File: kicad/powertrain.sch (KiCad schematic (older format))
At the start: 72 parts, among them P6 WR-TBL_691313710002, P7 CONN_01X02, P8 WR-TBL_691313710002, Q1 2N7002, U10 IFX007T, U11 74xx08, U5 LM358, U6 IFX007T, U7 IFX007T, U8 LM358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

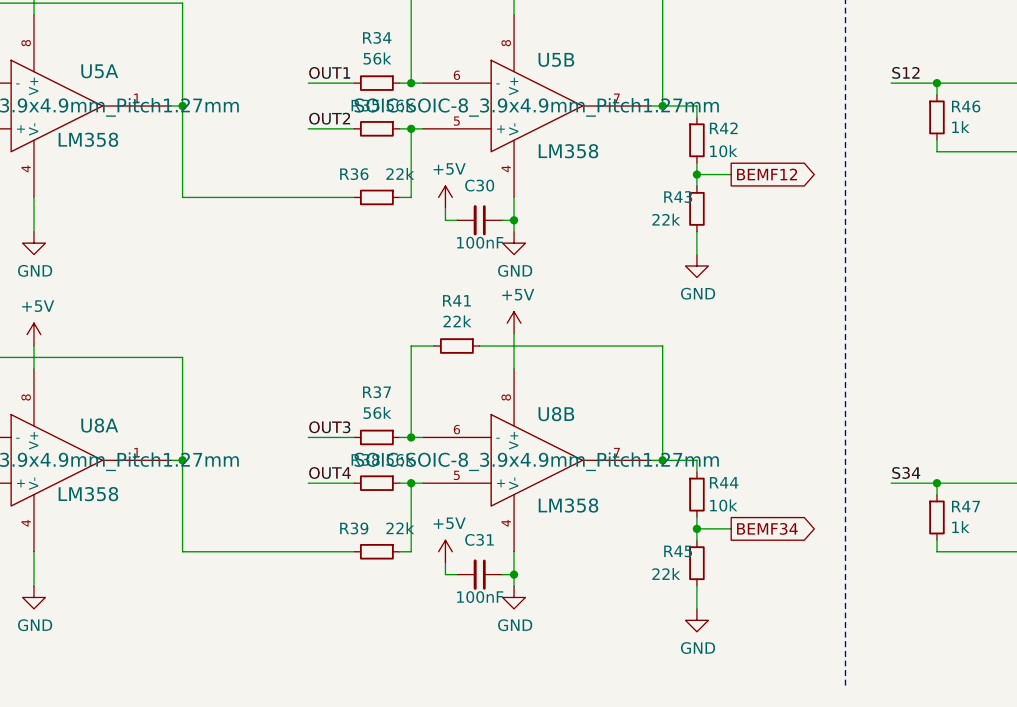
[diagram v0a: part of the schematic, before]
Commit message: added capacitors
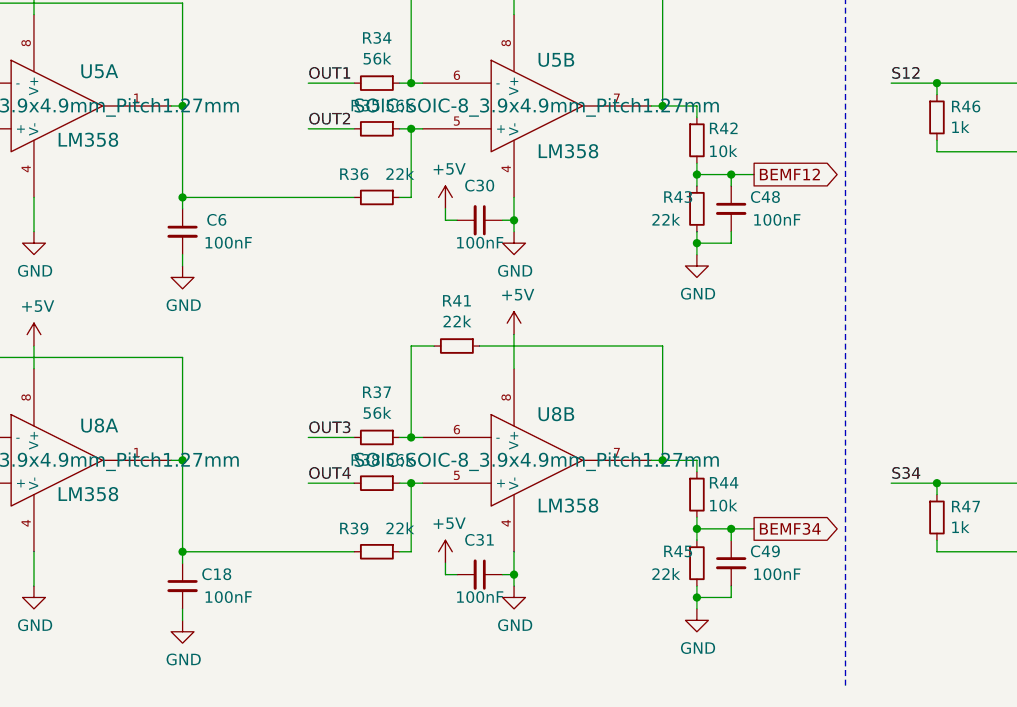
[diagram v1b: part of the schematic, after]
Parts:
- added C18, C48, C49, C6: 100nF, capacitors:C_0603, symbol devices:C_0603
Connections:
- net BEMF12: now also C48.1
- net BEMF34: now also C49.1
- net GND: now also C18.2, C48.2, C49.2, C6.2
- net at R36.2, U5.1, U5.2 (-): now also C6.1
- net at R39.2, U8.1, U8.2 (-): now also C18.1
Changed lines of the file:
@@
 	1    0    0    -1
 $EndComp
-Text GLabel 4950 7050 2    50   Output ~ 0
+Text GLabel 5050 7050 2    50   Output ~ 0
 BEMF34
 Connection ~ 4650 6750
@@
 	4800 6800 4800 6750
 Wire Wire Line
-	4800 7400 4800 7300
+	4800 7400 4800 7350
 Connection ~ 4000 7250
 Wire Wire Line
@@
 	1    0    0    -1
 $EndComp
-Wire Wire Line
-	4800 7050 4950 7050
 Wire Wire Line
 	4650 6250 3850 6250
@@
 	1    0    0    -1
 $EndComp
-Text GLabel 4950 5500 2    50   Output ~ 0
+Text GLabel 5050 5500 2    50   Output ~ 0
 BEMF12
 Connection ~ 4650 5200
@@
 	4800 5250 4800 5200
 Wire Wire Line
-	4800 5850 4800 5750
+	4800 5850 4800 5800
 Connection ~ 4000 5700
 Wire Wire Line
@@
 	1    0    0    -1
 $EndComp
+$Comp
+L devices:C_0603 C49
+U 1 1 5F6F6DBC
+P 4950 7200
+F 0 "C49" H 5100 7250 50  0000 C CNN
+F 1 "100nF" H 5150 7150 50  0000 C CNN
+F 2 "capacitors:C_0603" H 4950 7050 50  0001 C CNN
+F 3 "" H 4950 7200 50  0000 C CNN
+	1    4950 7200
+	1    0    0    -1
+$EndComp
+$Comp
+L devices:C_0603 C48
+U 1 1 5F7130B1
+P 4950 5650
+F 0 "C48" H 5100 5700 50  0000 C CNN
+F 1 "100nF" H 5150 5600 50  0000 C CNN
+F 2 "capacitors:C_0603" H 4950 5500 50  0001 C CNN
+F 3 "" H 4950 5650 50  0000 C CNN
+	1    4950 5650
+	1    0    0    -1
+$EndComp
+$Comp
+L devices:C_0603 C6
+U 1 1 5F72E83B
+P 2550 5750
+F 0 "C6" H 2700 5800 50  0000 C CNN
+F 1 "100nF" H 2750 5700 50  0000 C CNN
+F 2 "capacitors:C_0603" H 2550 5600 50  0001 C CNN
+F 3 "" H 2550 5750 50  0000 C CNN
+	1    2550 5750
+	1    0    0    -1
+$EndComp
+$Comp
+L devices:C_0603 C18
+U 1 1 5F749F41
+P 2550 7300
+F 0 "C18" H 2700 7350 50  0000 C CNN
+F 1 "100nF" H 2750 7250 50  0000 C CNN
+F 2 "capacitors:C_0603" H 2550 7150 50  0001 C CNN
+F 3 "" H 2550 7300 50  0000 C CNN
+	1    2550 7300
+	1    0    0    -1
+$EndComp
+Wire Wire Line
+	2550 7200 2550 7150
+Connection ~ 2550 7150
+Wire Wire Line
+	2550 5650 2550 5600
+Connection ~ 2550 5600
+Wire Wire Line
+	4950 5550 4950 5500
+Connection ~ 4950 5500
+Wire Wire Line
+	4950 5500 5050 5500
+Wire Wire Line
+	4800 5800 4950 5800
+Wire Wire Line
+	4950 5800 4950 5750
+Connection ~ 4800 5800
+Wire Wire Line
+	4800 5800 4800 5750
+Wire Wire Line
+	4800 7050 4950 7050
+Wire Wire Line
+	4950 7100 4950 7050
+Connection ~ 4950 7050
+Wire Wire Line
+	4950 7050 5050 7050
+Wire Wire Line
+	4950 7300 4950 7350
+Wire Wire Line
+	4950 7350 4800 7350
+Connection ~ 4800 7350
+Wire Wire Line
+	4800 7350 4800 7300
+$Comp
+L power-supply:GND #PWR0142
+U 1 1 5F82F73A
+P 2550 7450
+F 0 "#PWR0142" H 2550 7200 50  0001 C CNN
+F 1 "GND" H 2555 7277 50  0000 C CNN
+F 2 "" H 2550 7450 50  0000 C CNN
+F 3 "" H 2550 7450 50  0000 C CNN
+	1    2550 7450
+	1    0    0    -1
+$EndComp
+$Comp
+L power-supply:GND #PWR0147
+U 1 1 5F84D103
+P 2550 5900
+F 0 "#PWR0147" H 2550 5650 50  0001 C CNN
+F 1 "GND" H 2555 5727 50  0000 C CNN
+F 2 "" H 2550 5900 50  0000 C CNN
+F 3 "" H 2550 5900 50  0000 C CNN
+	1    2550 5900
+	1    0    0    -1
+$EndComp
+Wire Wire Line
+	2550 5900 2550 5850
+Wire Wire Line
+	2550 7450 2550 7400
 $EndSCHEMATC

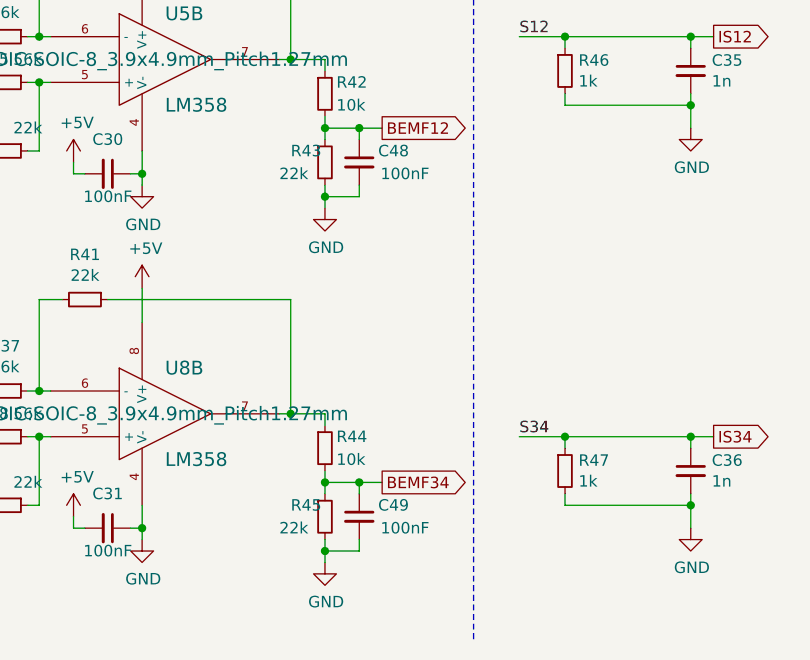
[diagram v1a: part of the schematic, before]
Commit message: added leds, updated capacitor values and changed silkscreen
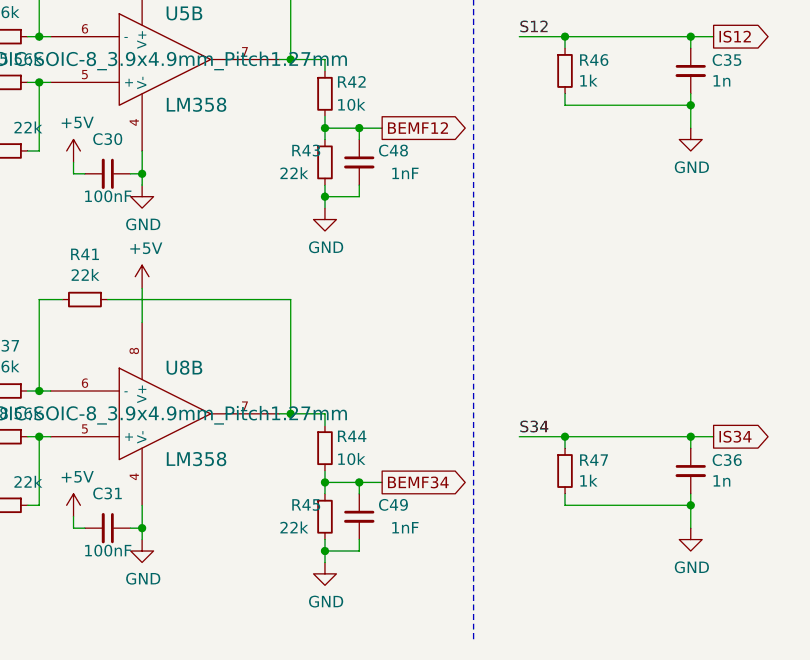
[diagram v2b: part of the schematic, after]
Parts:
- C48, C49: value 100nF -> 1nF
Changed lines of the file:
@@
 P 4950 7200
 F 0 "C49" H 5100 7250 50  0000 C CNN
-F 1 "100nF" H 5150 7150 50  0000 C CNN
+F 1 "1nF" H 5150 7150 50  0000 C CNN
 F 2 "capacitors:C_0603" H 4950 7050 50  0001 C CNN
 F 3 "" H 4950 7200 50  0000 C CNN
@@
 P 4950 5650
 F 0 "C48" H 5100 5700 50  0000 C CNN
-F 1 "100nF" H 5150 5600 50  0000 C CNN
+F 1 "1nF" H 5150 5600 50  0000 C CNN
 F 2 "capacitors:C_0603" H 4950 5500 50  0001 C CNN
 F 3 "" H 4950 5650 50  0000 C CNN

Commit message: bom update
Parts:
- C35, C36: value 1n -> 1nF
- C5: value 100 nF -> 100nF
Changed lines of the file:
@@
 P 6400 5250
 F 0 "C35" H 6492 5296 50  0000 L CNN
-F 1 "1n" H 6492 5205 50  0000 L CNN
+F 1 "1nF" H 6492 5205 50  0000 L CNN
 F 2 "capacitors:C_0603" H 6400 5100 50  0001 C CNN
 F 3 "" H 6400 5250 50  0000 C CNN
@@
 P 6400 7000
 F 0 "C36" H 6492 7046 50  0000 L CNN
-F 1 "1n" H 6492 6955 50  0000 L CNN
+F 1 "1nF" H 6492 6955 50  0000 L CNN
 F 2 "capacitors:C_0603" H 6400 6850 50  0001 C CNN
 F 3 "" H 6400 7000 50  0000 C CNN
@@
 P 8650 4900
 F 0 "C5" H 8742 4946 50  0000 L CNN
-F 1 "100 nF" H 8742 4855 50  0000 L CNN
+F 1 "100nF" H 8742 4855 50  0000 L CNN
 F 2 "capacitors:C_0603" H 8650 4750 50  0001 C CNN
 F 3 "" H 8650 4900 50  0000 C CNN

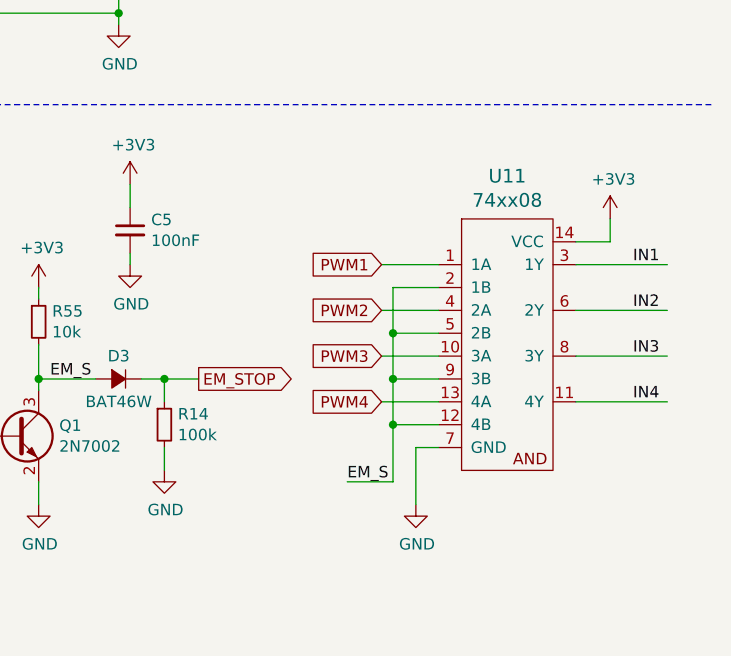
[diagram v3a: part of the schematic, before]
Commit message: improved emergency stop for breaking
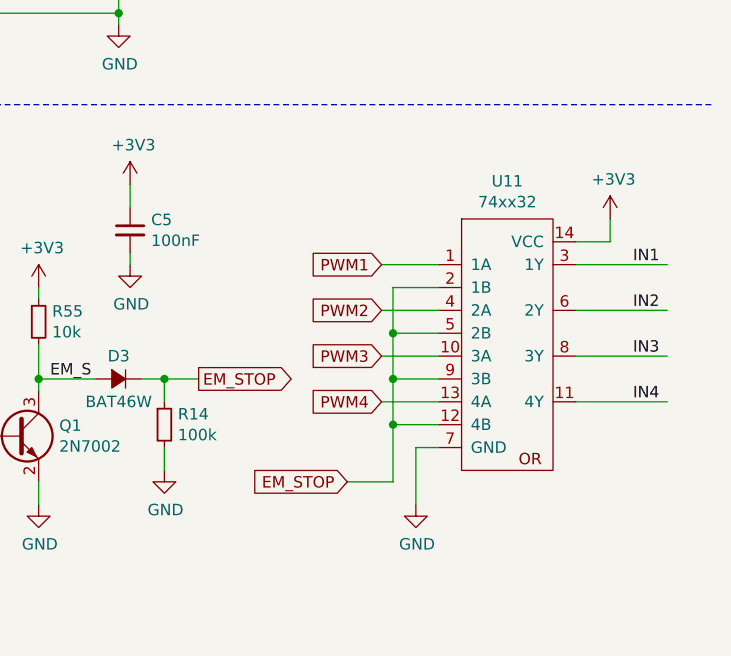
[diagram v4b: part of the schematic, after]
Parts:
- removed U11: 74xx08, SOIC:SOIC-14_3.9x8.7mm_Pitch1.27mm, symbol IC_logic:74xx08
- added U11: 74xx32, SOIC:SOIC-14_3.9x8.7mm_Pitch1.27mm, symbol IC_logic:74xx32
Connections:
- net +3V3: now also U11.14 (VCC)
- net EM_STOP: now also U11.12 (4B), U11.2 (1B), U11.5 (2B), U11.9 (3B)
- net GND: now also U11.7 (GND)
- net IN1: now also U11.3 (1Y)
- net IN2: now also U11.6 (2Y)
- net IN3: now also U11.8 (3Y)
- net IN4: now also U11.11 (4Y)
- net PWM1: now also U11.1 (1A)
- net PWM2: now also U11.4 (2A)
- net PWM3: now also U11.10 (3A)
- net PWM4: now also U11.13 (4A)
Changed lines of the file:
@@
 Text Label 6350 3100 0    50   ~ 0
 IN4
-$Comp
-L IC_logic:74xx08 U11
-U 1 1 5EF16DC4
-P 10100 5350
-F 0 "U11" H 10300 6037 60  0000 C CNN
-F 1 "74xx08" H 10300 5931 60  0000 C CNN
-F 2 "SOIC:SOIC-14_3.9x8.7mm_Pitch1.27mm" H 10400 5200 60  0001 C CNN
-F 3 "" H 10100 5350 60  0000 C CNN
-	1    10100 5350
-	1    0    0    -1
-$EndComp
 Text GLabel 9750 5050 0    50   Input ~ 0
 PWM1
@@
 Wire Wire Line
 	9600 6000 9800 6000
-Text Label 9600 6000 0    50   ~ 0
-EM_S
 $Comp
 L devices:R_0603 R14
@@
 Wire Wire Line
 	2550 7450 2550 7400
+Text GLabel 9600 6000 0    50   Input ~ 0
+EM_STOP
+$Comp
+L IC_logic:74xx32 U11
+U 1 1 5F7E0FEC
+P 10250 5950
+F 0 "U11" H 10300 7215 50  0000 C CNN
+F 1 "74xx32" H 10300 7124 50  0000 C CNN
+F 2 "SOIC:SOIC-14_3.9x8.7mm_Pitch1.27mm" H 10250 5950 50  0001 C CNN
+F 3 "" H 10250 5950 50  0001 C CNN
+	1    10250 5950
+	1    0    0    -1
+$EndComp
 $EndSCHEMATC

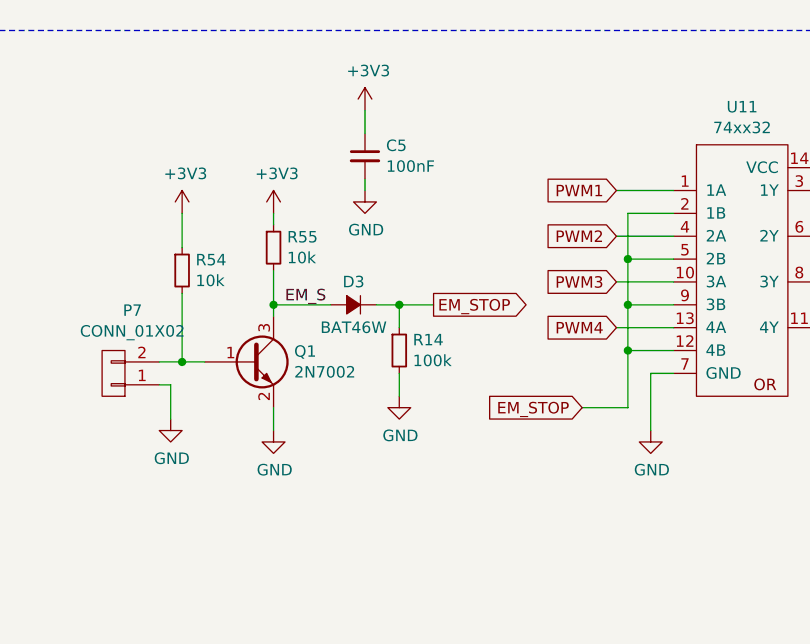
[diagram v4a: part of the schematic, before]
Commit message: improved emergency stop circuit for breaking
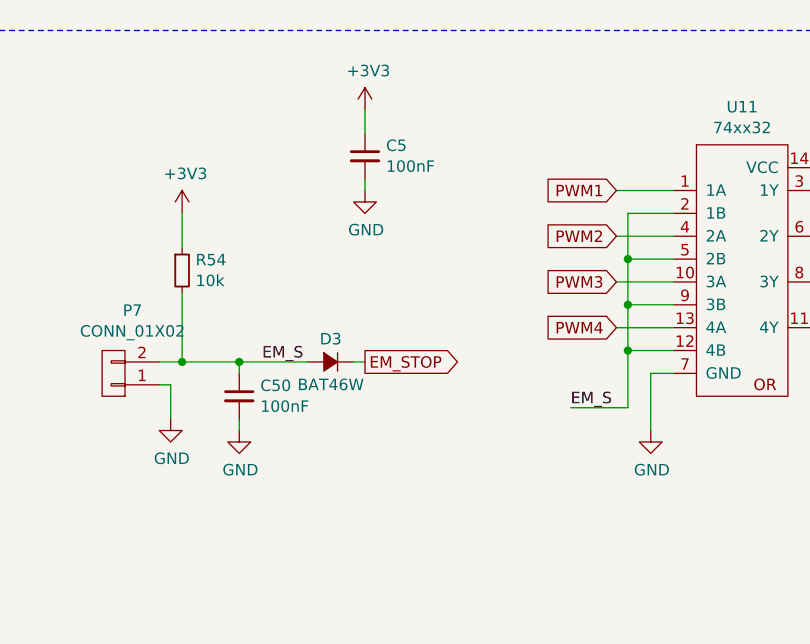
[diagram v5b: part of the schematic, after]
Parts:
- removed Q1: 2N7002, SOT_TO:SOT-23, symbol devices:Q_NPN_BEC
- removed R14: 100k, resistors:R_0603, symbol devices:R_0603
- removed R55: 10k, resistors:R_0603, symbol devices:R_0603
- added C50: 100nF, capacitors:C_0603, symbol devices:C_0603
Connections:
- net EM_S: now also P7.2 (P2), R54.2, U11.12 (4B), U11.2 (1B), U11.5 (2B), U11.9 (3B), C50.1
- net EM_STOP: no longer U11.12 (4B), U11.2 (1B), U11.5 (2B), U11.9 (3B)
- net GND: now also C50.2
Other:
- moved on the sheet: D3
